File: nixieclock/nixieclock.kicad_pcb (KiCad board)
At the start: 2 copper layers, 65 parts, among them Q1 IRLR3110ZTRPBF, Q2 AO3401A, Q3 BSS138, Q4 BSS138, Q5 BSS138, U1 LT3757AEMSE, U2 HV5522, U3 LMR64010XMF, U4 AMS1117-3.3, U5 HV5522

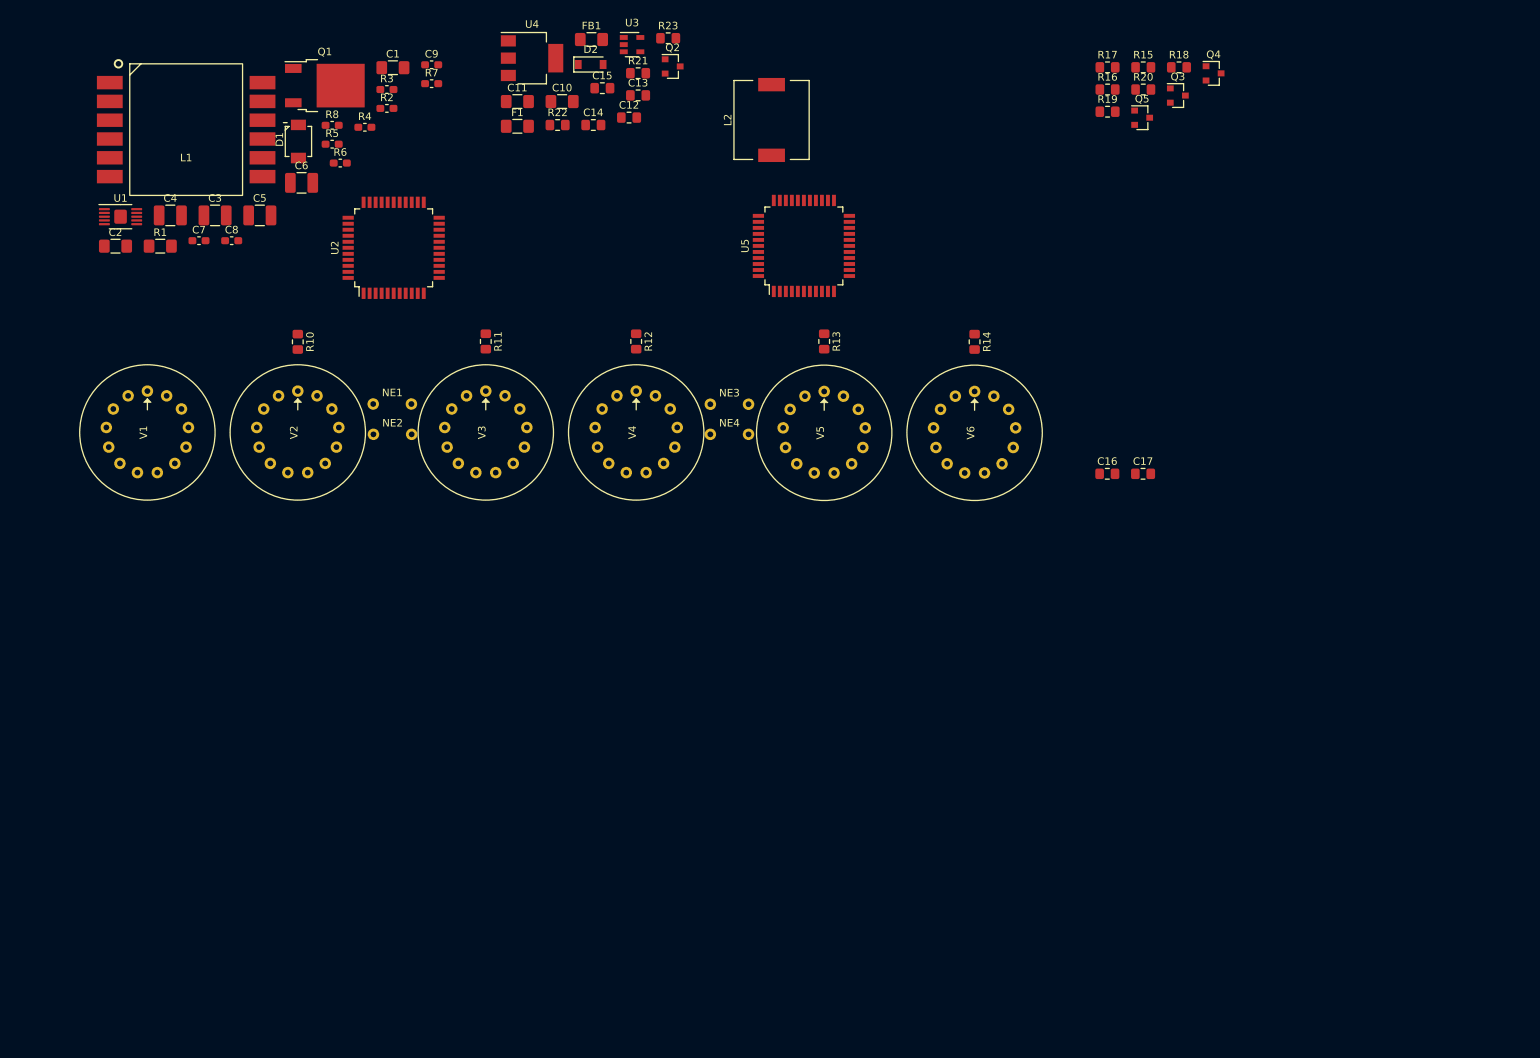
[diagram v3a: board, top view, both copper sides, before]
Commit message: began routing PCB, finalized registers design
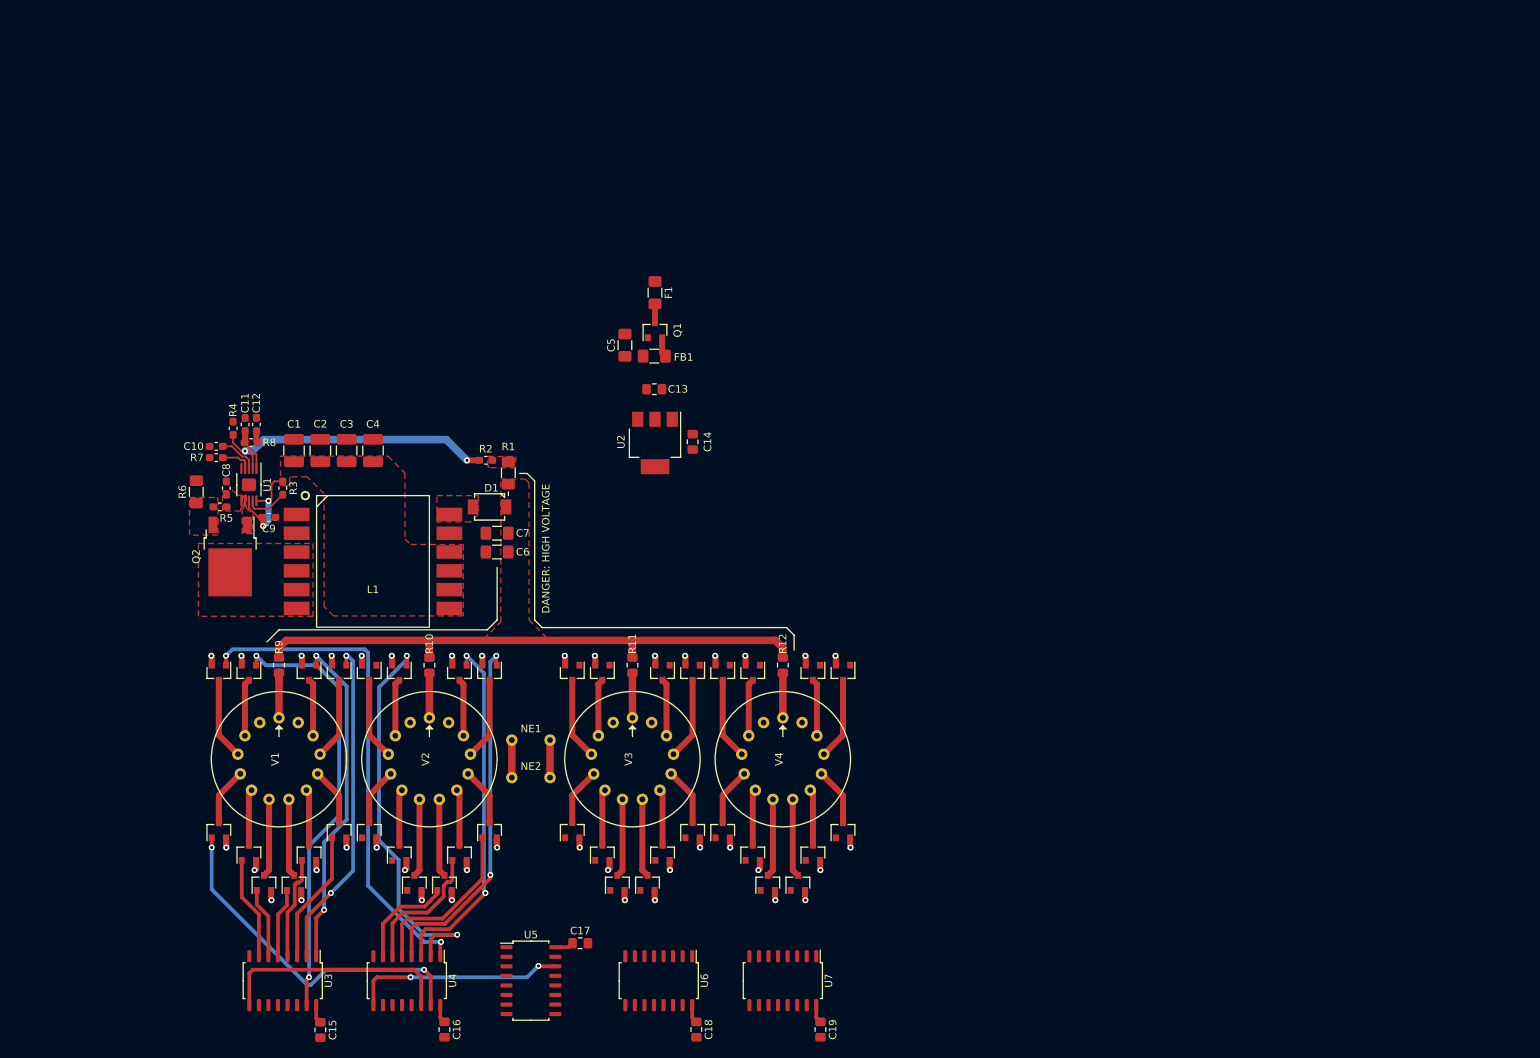
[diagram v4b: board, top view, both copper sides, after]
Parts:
- removed the C12 at (144.1, 72.7)
- removed the C13 at (145.2, 69.7)
- removed D2: MBR0520, Diode_SMD:D_SOD-123
- removed L2: 10uH, Personal:MSS1048-103MLB
- removed NE3, NE4: NE-2, Personal:NE-2
- removed R13, R14, R21: R, Resistor_SMD:R_0805_2012Metric_Pad1.15x1.40mm_HandSolder
- removed R15, R16, R17, R18, R19, R20: 2.21k, Resistor_SMD:R_0805_2012Metric_Pad1.15x1.40mm_HandSolder
- removed R22: 117k, Resistor_SMD:R_0805_2012Metric_Pad1.15x1.40mm_HandSolder
- removed R23: 13.3k, Resistor_SMD:R_0805_2012Metric_Pad1.15x1.40mm_HandSolder
- removed the U2 at (112.8, 90.0)
- removed V5, V6: IN14, Personal:IN-14
- added C15: 100nF, Capacitor_SMD:C_0805_2012Metric_Pad1.15x1.40mm_HandSolder, F.Cu at (103.0, 194.0)
- added C18: 100nF, Capacitor_SMD:C_0805_2012Metric_Pad1.15x1.40mm_HandSolder, F.Cu at (153.0, 193.9)
- added C19: 100nF, Capacitor_SMD:C_0805_2012Metric_Pad1.15x1.40mm_HandSolder, F.Cu at (169.5, 193.9)
- added C8: 10nF, Capacitor_SMD:C_0603_1608Metric_Pad1.05x0.95mm_HandSolder, F.Cu at (90.5, 122.0)
- added Q10: BSS131, Package_TO_SOT_SMD:SOT-23, F.Cu at (93.5, 170.4)
- added Q11: BSS131, Package_TO_SOT_SMD:SOT-23, F.Cu at (89.5, 167.4)
- added Q12: BSS131, Package_TO_SOT_SMD:SOT-23, F.Cu at (89.5, 146.5)
- added Q13: BSS131, Package_TO_SOT_SMD:SOT-23, F.Cu at (113.5, 146.5)
- added Q14: BSS131, Package_TO_SOT_SMD:SOT-23, F.Cu at (121.5, 146.5)
- added Q15: BSS131, Package_TO_SOT_SMD:SOT-23, F.Cu at (125.5, 146.5)
- added Q16: BSS131, Package_TO_SOT_SMD:SOT-23, F.Cu at (125.5, 167.4)
- added Q17: BSS131, Package_TO_SOT_SMD:SOT-23, F.Cu at (121.5, 170.4)
- added Q18: BSS131, Package_TO_SOT_SMD:SOT-23, F.Cu at (119.5, 174.4)
- added Q19: BSS131, Package_TO_SOT_SMD:SOT-23, F.Cu at (115.5, 174.4)
- added Q20: BSS131, Package_TO_SOT_SMD:SOT-23, F.Cu at (113.5, 170.4)
- added Q21: BSS131, Package_TO_SOT_SMD:SOT-23, F.Cu at (109.5, 167.4)
- added Q22: BSS131, Package_TO_SOT_SMD:SOT-23, F.Cu at (109.5, 146.5)
- added Q23: BSS131, Package_TO_SOT_SMD:SOT-23, F.Cu at (140.5, 146.5)
- added Q24: BSS131, Package_TO_SOT_SMD:SOT-23, F.Cu at (148.5, 146.5)
- added Q25: BSS131, Package_TO_SOT_SMD:SOT-23, F.Cu at (152.5, 146.5)
- added Q26: BSS131, Package_TO_SOT_SMD:SOT-23, F.Cu at (152.5, 167.4)
- added Q27: BSS131, Package_TO_SOT_SMD:SOT-23, F.Cu at (148.5, 170.4)
- added Q28: BSS131, Package_TO_SOT_SMD:SOT-23, F.Cu at (146.5, 174.4)
- added Q29: BSS131, Package_TO_SOT_SMD:SOT-23, F.Cu at (142.5, 174.4)
- added Q30: BSS131, Package_TO_SOT_SMD:SOT-23, F.Cu at (140.5, 170.4)
- added Q31: BSS131, Package_TO_SOT_SMD:SOT-23, F.Cu at (136.5, 167.4)
- added Q32: BSS131, Package_TO_SOT_SMD:SOT-23, F.Cu at (136.5, 146.5)
- added Q33: BSS131, Package_TO_SOT_SMD:SOT-23, F.Cu at (160.5, 146.5)
- added Q34: BSS131, Package_TO_SOT_SMD:SOT-23, F.Cu at (168.5, 146.5)
- added Q35: BSS131, Package_TO_SOT_SMD:SOT-23, F.Cu at (172.5, 146.5)
- added Q36: BSS131, Package_TO_SOT_SMD:SOT-23, F.Cu at (172.5, 167.4)
- added Q37: BSS131, Package_TO_SOT_SMD:SOT-23, F.Cu at (168.5, 170.4)
- added Q38: BSS131, Package_TO_SOT_SMD:SOT-23, F.Cu at (166.5, 174.4)
- added Q39: BSS131, Package_TO_SOT_SMD:SOT-23, F.Cu at (162.5, 174.4)
- added Q40: BSS131, Package_TO_SOT_SMD:SOT-23, F.Cu at (160.5, 170.4)
- added Q41: BSS131, Package_TO_SOT_SMD:SOT-23, F.Cu at (156.5, 167.4)
- added Q42: BSS131, Package_TO_SOT_SMD:SOT-23, F.Cu at (156.5, 146.5)
- added Q6: BSS131, Package_TO_SOT_SMD:SOT-23, F.Cu at (105.5, 167.4)
- added Q7: BSS131, Package_TO_SOT_SMD:SOT-23, F.Cu at (101.5, 170.4)
- added Q8: BSS131, Package_TO_SOT_SMD:SOT-23, F.Cu at (99.5, 174.4)
- added Q9: BSS131, Package_TO_SOT_SMD:SOT-23, F.Cu at (95.5, 174.4)
- added R9: 10k, Capacitor_SMD:C_0805_2012Metric_Pad1.15x1.40mm_HandSolder, F.Cu at (97.5, 145.5)
- added U4: 74HC595, Package_SO:SOIC-16_4.55x10.3mm_P1.27mm, F.Cu at (114.5, 187.4)
- added U6: 74HC595, Package_SO:SOIC-16_4.55x10.3mm_P1.27mm, F.Cu at (148.0, 187.4)
- added U7: 74HC595, Package_SO:SOIC-16_4.55x10.3mm_P1.27mm, F.Cu at (164.5, 187.4)
- C11: value 4.7uF -> 100pF; footprint Capacitor_SMD:C_1206_3216Metric_Pad1.42x1.75mm_HandSolder -> Capacitor_SMD:C_0603_1608Metric_Pad1.05x0.95mm_HandSolder
- Q3, Q4, Q5: value BSS138 -> BSS131
- R6: footprint Resistor_SMD:R_0603_1608Metric_Pad1.05x0.95mm_HandSolder -> Resistor_SMD:R_1206_3216Metric_Pad1.42x1.75mm_HandSolder
- U3: value LMR64010XMF -> 74HC595; footprint Package_TO_SOT_SMD:SOT-23-5 -> Package_SO:SOIC-16_4.55x10.3mm_P1.27mm
- U5: value HV5522 -> 74HC595; footprint Package_QFP:PQFP-44_10x10mm_P0.8mm -> Package_SO:SOIC-16_4.55x10.3mm_P1.27mm
- moved Q3 145.4 mm to (93.5, 146.5), turned to -90 degrees
- moved Q4 144.3 mm to (101.5, 146.5), turned to -90 degrees
- moved U3 132.9 mm to (98.0, 187.4), turned to -90 degrees
- moved Q5 129.8 mm to (105.5, 146.5), turned to -90 degrees
- moved C16 115.0 mm to (119.5, 193.9), turned to -90 degrees
- moved U5 104.2 mm to (131.0, 187.4), turned to 0 degrees
- moved C17 97.5 mm to (137.6, 182.5)
- moved C6 65.9 mm to (126.5, 130.4), turned to 180 degrees
- moved Q2 63.9 mm to (91.0, 131.1), turned to -90 degrees
- moved C7 63.5 mm to (126.5, 127.9), turned to 180 degrees
- moved L1 62.6 mm to (110.0, 131.9)
- moved R7 57.4 mm to (89.1, 117.9), turned to 180 degrees
- moved C11 56.2 mm to (93.0, 113.5), turned to 90 degrees
- moved R1 55.3 mm to (128.0, 120.0), turned to 90 degrees
- moved D1 54.8 mm to (125.5, 124.5), turned to -90 degrees
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- renumbered C3 to C1, C8 to C10, C9 to C12, C14 to C13, C15 to C14, C4 to C2, C5 to C3, C6 to C4, C10 to C5, C1 to C6, C2 to C7, C7 to C9, Q2 to Q1, Q1 to Q2, U4 to U2
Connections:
- C11 pad 1: +12V -> Net-(C11-Pad1)
- C16 pad 1: +12V -> +3V3
- C17 pad 1: +12V -> +3V3
- Q3 pad 1: Net-(Q3-Pad1) -> /cathode_registers/GA0
- Q3 pad 3: /cathode_registers/HV_DIN -> /cathode_sinks/NA0
- Q4 pad 1: Net-(Q4-Pad1) -> /cathode_registers/GA1
- Q4 pad 3: /cathode_registers/HV_CLK -> /cathode_sinks/NA1
- Q5 pad 1: Net-(Q5-Pad1) -> /cathode_registers/GA2
- Q5 pad 3: /cathode_registers/~HV_LE -> /cathode_sinks/NA2
- R8 pad 1: Net-(R8-Pad1) -> Net-(C11-Pad1)
- U1 pad 1: Net-(R8-Pad1) -> Net-(C11-Pad1)
- U3 pad 1: Net-(D2-Pad2) -> /cathode_registers/GA1
- U3 pad 2: GND -> /cathode_registers/GA2
- U3 pad 3: Net-(C13-Pad2) -> /cathode_registers/GA3
- U3 pad 4: ~SHDN -> /cathode_registers/GA4
- U3 pad 5: VCC -> /cathode_registers/GA5
- U5 pad 1: /NE7 -> /cathode_registers/GB7
- U5 pad 10: /NF8 -> /cathode_registers/~RES
- U5 pad 11: /NF7 -> /cathode_registers/CLK
- U5 pad 12: /NF6 -> /cathode_registers/LCLK
- U5 pad 13: /NF5 -> /cathode_registers/~OE
- U5 pad 14: /NF4 -> Net-(U4-Pad9)
- U5 pad 15: /NF3 -> /cathode_registers/GB6
- U5 pad 16: /NF2 -> +3V3
- U5 pad 2: /NE6 -> /cathode_registers/GB8
- U5 pad 3: /NE5 -> /cathode_registers/GB9
- U5 pad 4: /NE4 -> /cathode_registers/GC0
- U5 pad 5: /NE3 -> /cathode_registers/GC1
- U5 pad 6: /NE2 -> /cathode_registers/GC2
- U5 pad 7: /NE1 -> /cathode_registers/GC3
- U5 pad 8: /NE0 -> GND
- U5 pad 9: /NF9 -> Net-(U5-Pad9)
- V1 pad 1: (no net) -> Net-(R9-Pad2)
- V1 pad 10: /NA8 -> /cathode_sinks/NA8
- V1 pad 11: /NA9 -> /cathode_sinks/NA9
- V1 pad 12: /NA0 -> /cathode_sinks/NA0
- V1 pad 3: /NA1 -> /cathode_sinks/NA1
- V1 pad 4: /NA2 -> /cathode_sinks/NA2
- V1 pad 5: /NA3 -> /cathode_sinks/NA3
- V1 pad 6: /NA4 -> /cathode_sinks/NA4
- V1 pad 7: /NA5 -> /cathode_sinks/NA5
- V1 pad 8: /NA6 -> /cathode_sinks/NA6
- V1 pad 9: /NA7 -> /cathode_sinks/NA7
- V2 pad 10: /NB8 -> /cathode_sinks/NB8
- V2 pad 11: /NB9 -> /cathode_sinks/NB9
- V2 pad 12: /NB0 -> /cathode_sinks/NB0
- V2 pad 3: /NB1 -> /cathode_sinks/NB1
- V2 pad 4: /NB2 -> /cathode_sinks/NB2
- V2 pad 5: /NB3 -> /cathode_sinks/NB3
- V2 pad 6: /NB4 -> /cathode_sinks/NB4
- V2 pad 7: /NB5 -> /cathode_sinks/NB5
- V2 pad 8: /NB6 -> /cathode_sinks/NB6
- V2 pad 9: /NB7 -> /cathode_sinks/NB7
- V3 pad 10: /NC8 -> /cathode_sinks/NC8
- V3 pad 11: /NC9 -> /cathode_sinks/NC9
- V3 pad 12: /NC0 -> /cathode_sinks/NC0
- V3 pad 3: /NC1 -> /cathode_sinks/NC1
- V3 pad 4: /NC2 -> /cathode_sinks/NC2
- V3 pad 5: /NC3 -> /cathode_sinks/NC3
- V3 pad 6: /NC4 -> /cathode_sinks/NC4
- V3 pad 7: /NC5 -> /cathode_sinks/NC5
- V3 pad 8: /NC6 -> /cathode_sinks/NC6
- V3 pad 9: /NC7 -> /cathode_sinks/NC7
- V4 pad 10: /ND8 -> /cathode_sinks/ND8
- V4 pad 11: /ND9 -> /cathode_sinks/ND9
- V4 pad 12: /ND0 -> /cathode_sinks/ND0
- V4 pad 3: /ND1 -> /cathode_sinks/ND1
- V4 pad 4: /ND2 -> /cathode_sinks/ND2
- V4 pad 5: /ND3 -> /cathode_sinks/ND3
- V4 pad 6: /ND4 -> /cathode_sinks/ND4
- V4 pad 7: /ND5 -> /cathode_sinks/ND5
- V4 pad 8: /ND6 -> /cathode_sinks/ND6
- V4 pad 9: /ND7 -> /cathode_sinks/ND7
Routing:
- net HV: track 0.00 -> 74.6 mm
- net /cathode_registers/GA9: track 0.00 -> 66.4 mm, vias 0 -> 2
- net /cathode_registers/GA0: track 0.00 -> 58.0 mm, vias 0 -> 2
- net /cathode_registers/GB0: track 0.00 -> 52.8 mm, vias 0 -> 2
- net GND: track 0.00 -> 52.3 mm, vias 0 -> 40
- net /cathode_registers/GB2: track 0.00 -> 48.1 mm, vias 0 -> 2
- net /cathode_registers/GB1: track 0.00 -> 47.6 mm, vias 0 -> 2
- net /cathode_registers/GA8: track 0.00 -> 46.3 mm, vias 0 -> 2
- net /cathode_registers/GA1: track 0.00 -> 44.6 mm, vias 0 -> 2
- net /cathode_registers/GA2: track 0.00 -> 44.2 mm, vias 0 -> 2
- net /power_supply/FBX: track 0.00 -> 39.0 mm, vias 0 -> 2
- net Net-(U3-Pad9): track 0.00 -> 31.5 mm
- net Net-(U4-Pad9): track 0.00 -> 28.3 mm, vias 0 -> 2
- net /cathode_registers/GB3: track 0.00 -> 22.9 mm
- net /cathode_registers/GB4: track 0.00 -> 18.2 mm
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- added copper zone on F.Cu, net HV
- added copper zone on F.Cu, net Net-(C8-Pad1)
- added copper zone on F.Cu, net Net-(D1-Pad2)
- added copper zone on F.Cu, net Net-(L1-Pad3)
- added copper zone on F.Cu, net Net-(Q2-Pad1)
- added copper zone on F.Cu, net Net-(Q2-Pad3)
- added copper zone on F.Cu, net Net-(R1-Pad2)
- added copper zone on F.Cu, net VCC
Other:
- copper layers 2 -> 4
- board text added: "DANGER: HIGH VOLTAGE"

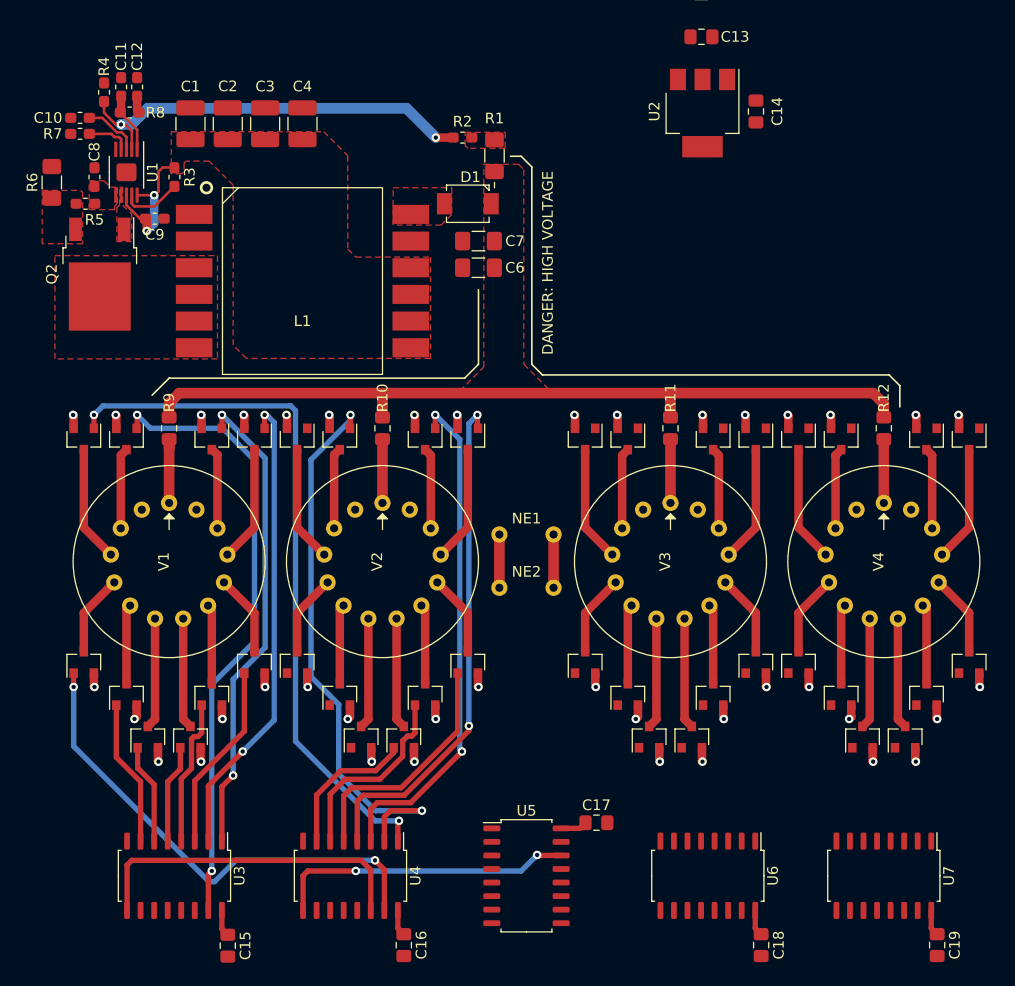
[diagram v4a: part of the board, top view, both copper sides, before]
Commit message: began work on microcontroller (stm32f0)
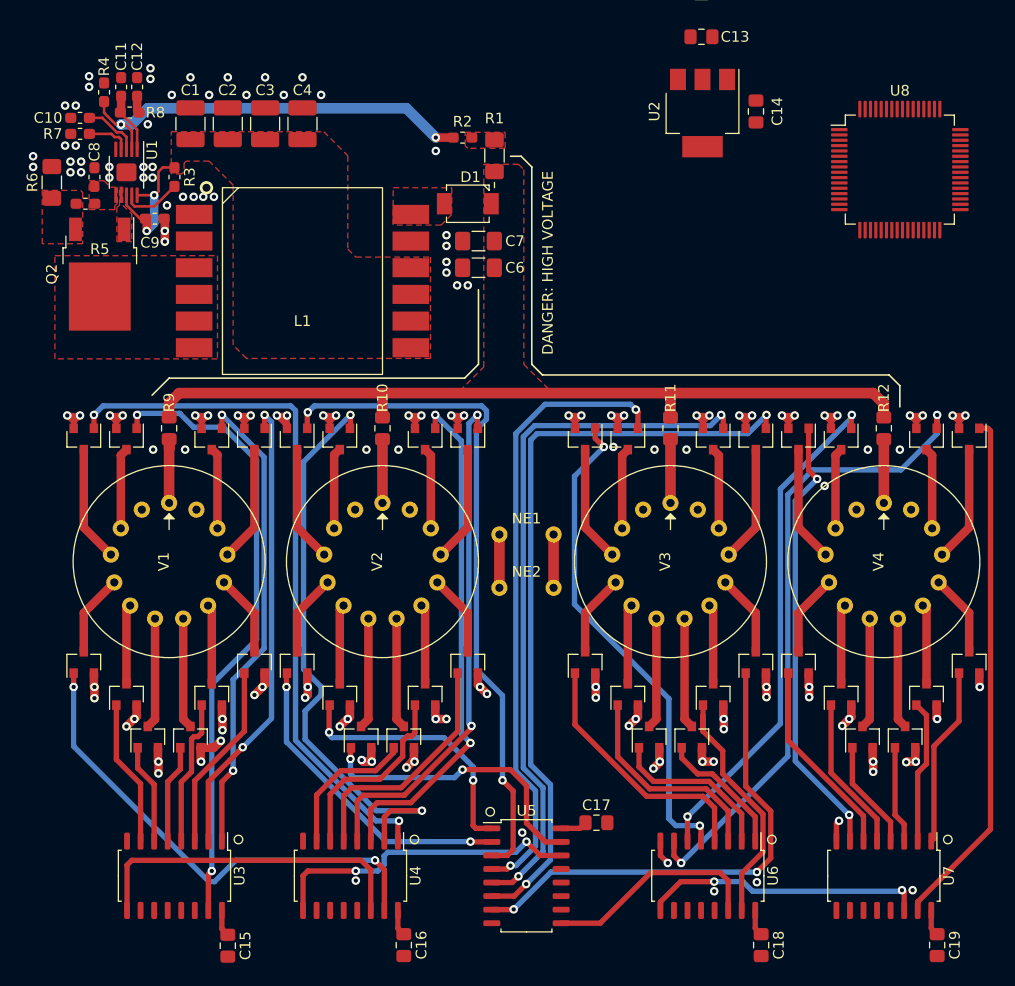
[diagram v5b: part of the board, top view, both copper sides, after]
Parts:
- added U8: STM32F058R8Tx, Package_QFP:LQFP-64_10x10mm_P0.5mm, F.Cu at (166.0, 121.2)
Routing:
- net /cathode_registers/GC2: track 0.00 -> 71.4 mm, vias 0 -> 2
- net GND: track 52.3 -> 119.1 mm, vias 40 -> 139
- net /cathode_registers/GC1: track 0.00 -> 66.4 mm, vias 0 -> 2
- net /cathode_registers/GB9: track 0.00 -> 63.9 mm, vias 0 -> 2
- net /cathode_registers/GD1: track 0.00 -> 60.4 mm, vias 0 -> 2
- net /cathode_registers/GC0: track 0.00 -> 58.8 mm, vias 0 -> 2
- net /cathode_registers/GC9: track 0.00 -> 49.4 mm, vias 0 -> 2
- net /cathode_registers/GD2: track 0.00 -> 49.1 mm
- net /cathode_registers/GD0: track 0.00 -> 47.6 mm, vias 0 -> 2
- net /cathode_registers/GC3: track 0.00 -> 46.5 mm, vias 0 -> 2
- net /cathode_registers/GD9: track 0.00 -> 42.0 mm, vias 0 -> 2
- net /cathode_registers/GB8: track 0.00 -> 29.6 mm, vias 0 -> 2
- net /cathode_registers/GB6: track 0.00 -> 27.5 mm, vias 0 -> 2
- net Net-(U6-Pad9): track 0.00 -> 26.6 mm, vias 0 -> 2
- net /cathode_registers/GB7: track 0.00 -> 24.9 mm, vias 0 -> 2
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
